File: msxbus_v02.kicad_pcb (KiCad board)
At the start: 2 copper layers, 4 parts, among them J1 RPi_GPIO, P1 MSX_SLOT, P2 MSX_SLOT, U1 CPLD

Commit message: PCB update
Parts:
- moved P2 14.0 mm to (143.5, 102.9)
- moved U1 14.0 mm to (147.3, 78.7)
- moved P1 14.0 mm to (143.5, 135.9)
- moved J1 14.0 mm to (151.1, 47.0)
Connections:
- P1 pad 44: /SW1 -> /SWOUT
- P1 pad 46: /SW2 -> /SW1
- P2 pad 4: /SLTSL1 -> /SLTSL2
- P2 pad 44: /SW1 -> /SWOUT
- U1 pad 1: Net-(U1-Pad1) -> /GND
- U1 pad 10: /RG15 -> /RG27
- U1 pad 11: /RG17 -> /RG22
- U1 pad 12: /RG18 -> /RG23
- U1 pad 13: /RG27 -> /RG24
- U1 pad 14: /RG22 -> /RG10
- U1 pad 15: /RG23 -> /RG09
- U1 pad 16: /RG24 -> /RG25
- U1 pad 17: /RG10 -> /RG11
- U1 pad 18: /RG09 -> /RG08
- U1 pad 19: /RG25 -> /RG07
- U1 pad 2: Net-(U1-Pad2) -> /GND
- U1 pad 20: /RG11 -> /RG00
- U1 pad 21: /RG08 -> /RG01
- U1 pad 22: /RG07 -> /RG05
- U1 pad 23: /RG00 -> /RG06
- U1 pad 24: /RG01 -> /RG12
- U1 pad 25: /RG05 -> /RG13
- U1 pad 26: /RG06 -> /RG19
- U1 pad 27: /RG12 -> /RG16
- U1 pad 28: /RG13 -> /RG26
- U1 pad 29: /RG19 -> /RG20
- U1 pad 3: Net-(U1-Pad3) -> /RG02
- U1 pad 30: /RG16 -> /RG21
- U1 pad 31: /RG26 -> Net-(U1-Pad31)
- U1 pad 32: /RG20 -> Net-(U1-Pad32)
- U1 pad 33: /RG21 -> Net-(U1-Pad33)
- U1 pad 34: /RG04 -> Net-(U1-Pad34)
- U1 pad 4: Net-(U1-Pad4) -> /RG03
- U1 pad 41: Net-(U1-Pad41) -> /SW2
- U1 pad 42: Net-(U1-Pad42) -> /SW1
- U1 pad 44: Net-(U1-Pad44) -> /GND
- U1 pad 45: /SW1 -> /SWOUT
- U1 pad 46: /SW2 -> /CLOCK
- U1 pad 47: /SWOUT -> /D6
- U1 pad 48: /CLOCK -> /D7
- U1 pad 49: /D6 -> /D4
- U1 pad 5: Net-(U1-Pad5) -> /RG04
- U1 pad 50: /D7 -> /D5
- U1 pad 6: /RG02 -> /RG14
- U1 pad 7: /RG03 -> /RG15
- U1 pad 8: /RG04 -> /RG17
- U1 pad 9: /RG14 -> /RG18
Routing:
- net /D7: track 0.00 -> 44.0 mm
- net /RG26: track 0.00 -> 21.2 mm
- net /RG19: track 0.00 -> 21.2 mm
- net /RG21: track 0.00 -> 20.9 mm
- net /RG05: track 0.00 -> 19.4 mm
- net /RG00: track 0.00 -> 19.4 mm
- net /RG10: track 0.00 -> 18.4 mm
- net /RG27: track 0.00 -> 17.3 mm
- net /RG17: track 0.00 -> 17.3 mm
- net /RG13: track 0.00 -> 16.9 mm
- net /RG12: track 0.00 -> 16.9 mm
- net /RG06: track 0.00 -> 16.9 mm
- net /RG03: track 0.00 -> 16.3 mm
- net /RG11: track 0.00 -> 15.9 mm
- net /RG08: track 0.00 -> 15.9 mm
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- added copper zone on B.Cu, net /GND
- added copper zone on F.Cu, net /GND
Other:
- net class Default: clearance 0.2 -> 0.18; trace_width 0.25 -> 0.22
- rule trace_clearance: 0.2 -> 0.18

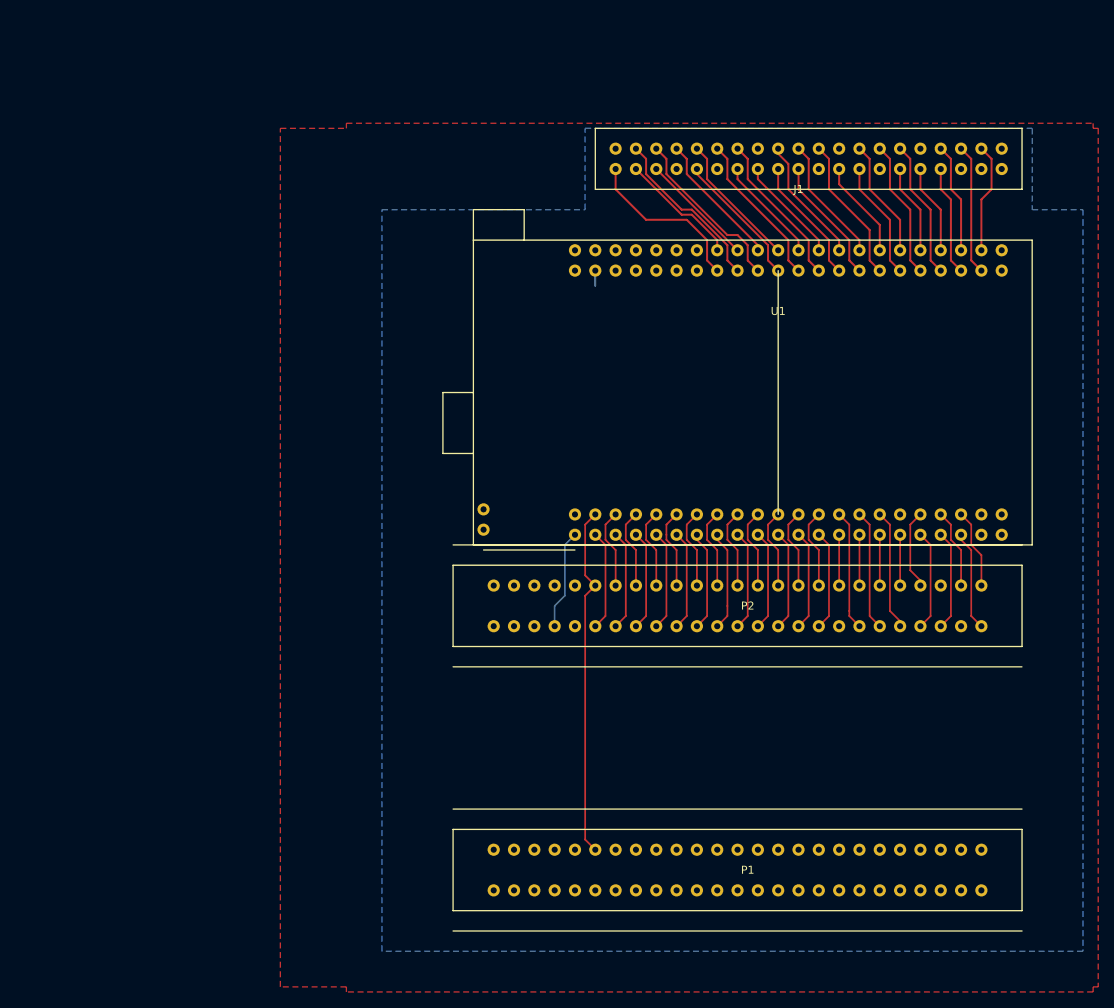
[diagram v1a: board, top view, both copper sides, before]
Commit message: update for MSXBUS v0.6
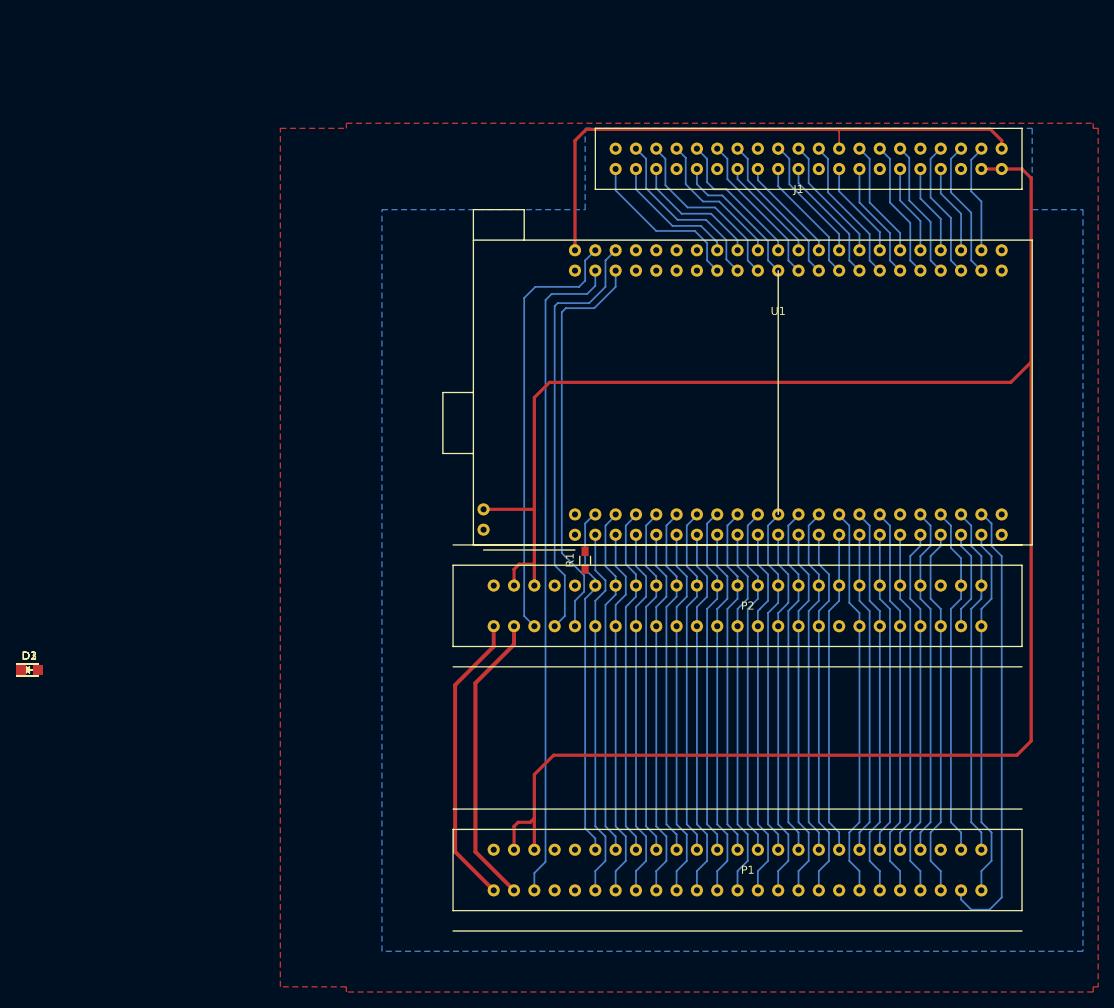
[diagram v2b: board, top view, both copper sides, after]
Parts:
- added D1, D2, D3: LED, LEDs:LED_0805, F.Cu at (53.7, 110.9)
- added R1: R, Resistors_SMD:R_0603_HandSoldering, F.Cu at (123.2, 97.2)
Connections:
- P1 pad 2: /C2 -> /CS2
- P1 pad 48: Net-(P1-Pad48) -> /+V12
- P1 pad 50: Net-(P1-Pad50) -> /-V12
- P2 pad 2: /C2 -> /CS2
- P2 pad 48: Net-(P2-Pad48) -> /+V12
- P2 pad 50: Net-(P2-Pad50) -> /-V12
- U1 pad 39: Net-(U1-Pad39) -> /SWOUT
- U1 pad 40: Net-(U1-Pad40) -> /CLOCK
- U1 pad 45: /SWOUT -> /GND
- U1 pad 46: /CLOCK -> /3V3
- U1 pad 5: /RG04 -> /RG14
- U1 pad 54: /D1 -> /D1_
- U1 pad 6: /RG14 -> /RG04
- U1 pad 83: /CS2 -> /SLTSL2
- U1 pad 85: /SLTSL2 -> /CS2
- U1 pad 89: (no net) -> /5V
- U1 pad 90: (no net) -> /GND
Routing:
- net /5V: track 0.00 -> 254.8 mm
- net /SW1: track 3.81 -> 83.2 mm
- net /3V3: track 0.00 -> 71.7 mm
- net /SLTSL1: track 0.00 -> 56.4 mm
- net /SW2: track 0.00 -> 54.4 mm
- net /CLOCK: track 0.00 -> 51.0 mm
- net /SWOUT: track 12.5 -> 53.5 mm
- net /-V12: track 0.00 -> 37.0 mm
- net /+V12: track 0.00 -> 37.0 mm
- net /CS2: track 10.7 -> 46.6 mm
- net /A1: track 9.94 -> 44.1 mm
- net /WAIT: track 9.94 -> 44.0 mm
- net /A8: track 12.5 -> 46.6 mm
- net /A6: track 12.5 -> 46.6 mm
- net /A2: track 12.5 -> 46.6 mm
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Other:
- net class V12 added: clearance 0.18, trace_width 0.5, via_dia 0.6, via_drill 0.4
- net class V5 added: clearance 0.18, trace_width 0.4, via_dia 0.6, via_drill 0.4

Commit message: minor update
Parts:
- moved D3 57.5 mm to (100.8, 78.0)
- moved D1 54.1 mm to (101.0, 84.6)
- moved D2 52.5 mm to (101.6, 89.4)
- moved R1 32.8 mm to (129.7, 65.0)
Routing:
- net /5V: track 254.8 -> 122.8 mm
- net /SW1: track 83.2 -> 0.00 mm
- net /SW2: track 54.4 -> 0.00 mm
- net /SWOUT: track 53.5 -> 0.00 mm
- net /CLOCK: track 51.0 -> 0.00 mm
- net /D1_: track 7.00 -> 1.92 mm
- net /D1: track 37.0 -> 42.1 mm
- net /3V3: track 71.7 -> 67.1 mm
